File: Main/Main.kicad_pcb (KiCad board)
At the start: 2 copper layers, 76.2 x 76.2 mm, 71 parts, among them J3 Conn_01x03, J4 Conn_01x03, J5 Conn_01x03, J6 Conn_01x03, U1 RP2350A-QFN60, U10 LM75B, U11 MCS1802GS-50-Z, U12 MCS1802GS-50-Z, U13 MCS1802GS-50-Z, U2 W25Q128JVS, U3 AMS1117-3.3, U4 MMC5983MA, U5 ICM-42688-P, U6 INA226, U7 KX134-1211, U8 MS5611-01BA, U9 MCS1802GS-50-Z, Y1 ABM8-272-T3

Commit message: Layout/Footprint Updates
updated footprint of inductor for R-Pi, started planning layout for R-PI components in middle of board, added two options for board size
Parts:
- added G***: LOGO, logos:ECLIPSELogo1, F.Cu at (100.0, 125.0)
- C10, C11, C12, C13, C14, C15, C16, C17, C18, C19, C20, C21, C22, C23, C24, C25, C26, C27, C28, C29, C30, C31, C32, C33, C34, C5, C6, C7, C8, C9: footprint Capacitor_SMD:C_0805_2012Metric -> Capacitor_SMD:C_0603_1608Metric
- L1: footprint Inductor_SMD:L_0805_2012Metric -> otherComponents:AOTA-B201610S3R3-101-T(L_0806_2016metric)
- R10, R11, R12, R2, R3, R4, R5, R6, R7, R8: footprint Resistor_SMD:R_0805_2012Metric -> Resistor_SMD:R_0603_1608Metric
- moved C17 175.9 mm to (108.2, 106.2), turned to 135 degrees
- moved C16 168.9 mm to (104.0, 110.5), turned to -45 degrees
- moved R1 148.8 mm to (98.4, 91.9), turned to -45 degrees
- moved C4 143.7 mm to (104.5, 103.8), turned to -45 degrees
- moved L1 143.0 mm to (96.4, 93.7), turned to 45 degrees
- moved C1 137.1 mm to (98.2, 95.3), turned to 45 degrees
- moved C2 135.0 mm to (97.5, 94.7), turned to 45 degrees
- moved C3 134.9 mm to (99.8, 93.2), turned to -45 degrees
- moved R6 44.3 mm to (103.8, 104.8)
- moved Y1 40.2 mm to (106.2, 108.5), turned to 45 degrees
- moved U4 38.9 mm to (65.3, 57.0)
- moved U5 38.9 mm to (70.6, 62.2)
- moved U7 38.9 mm to (65.8, 64.5)
- moved U8 38.9 mm to (70.3, 55.8)
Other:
- board size 76.2 x 76.2 mm -> 176.9 x 76.2 mm

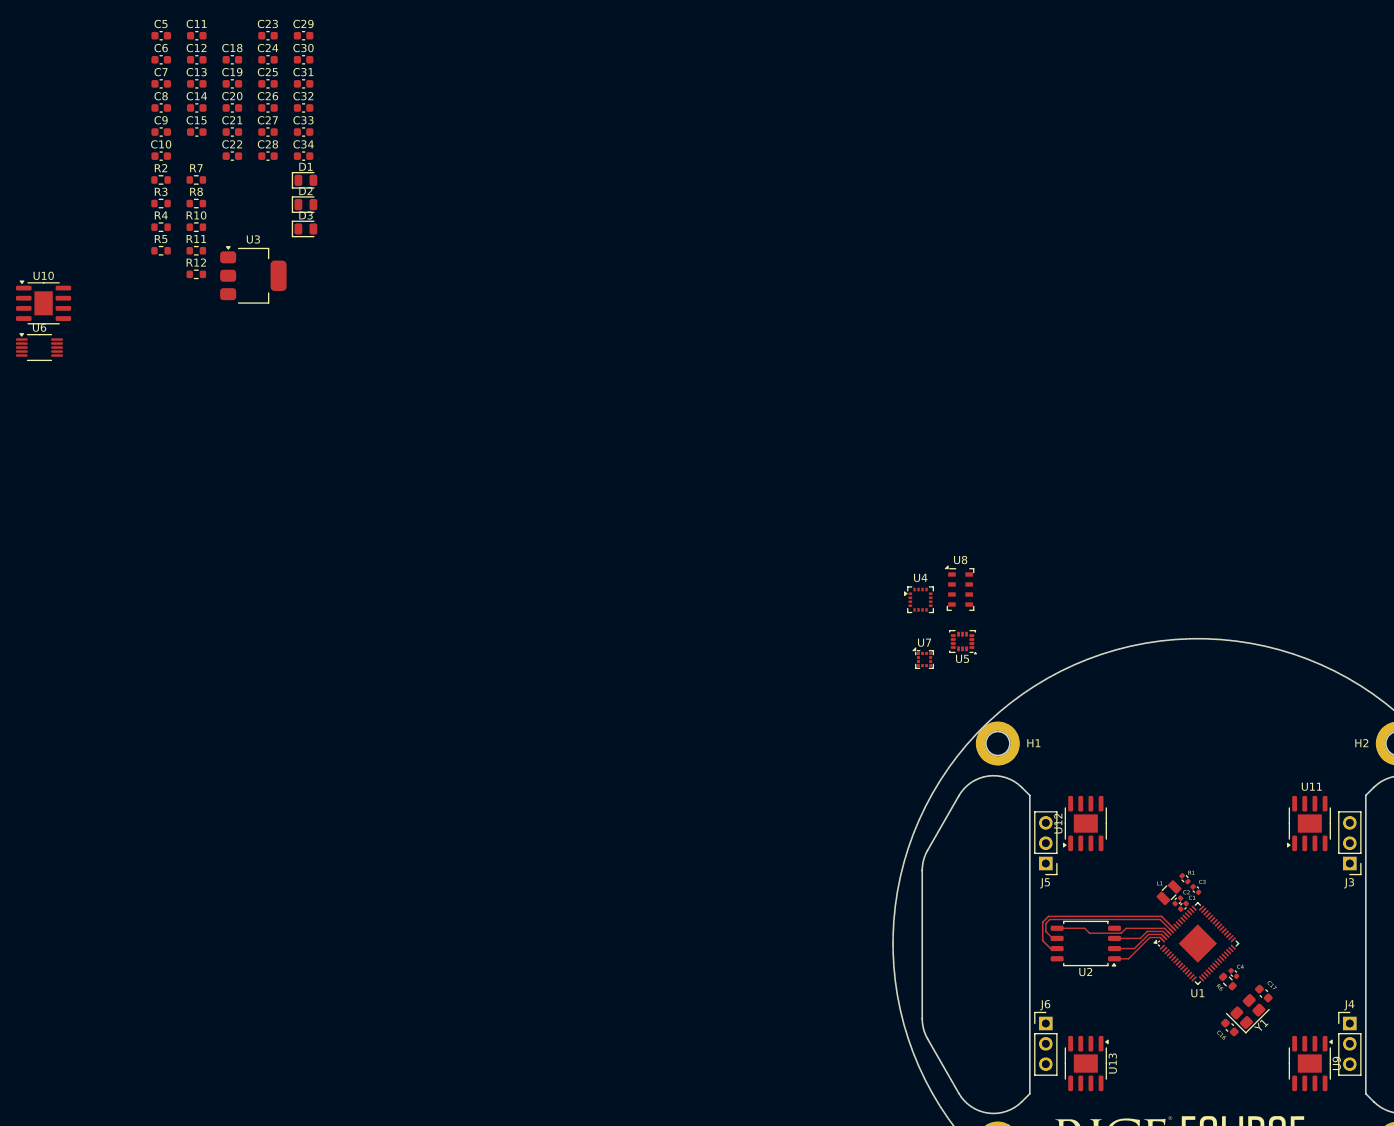
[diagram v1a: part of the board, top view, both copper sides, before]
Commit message: More RP2350 Footprint
put more footprints in place(mostly power), updated things to 0402 where possible, and added switching regulator to schematic
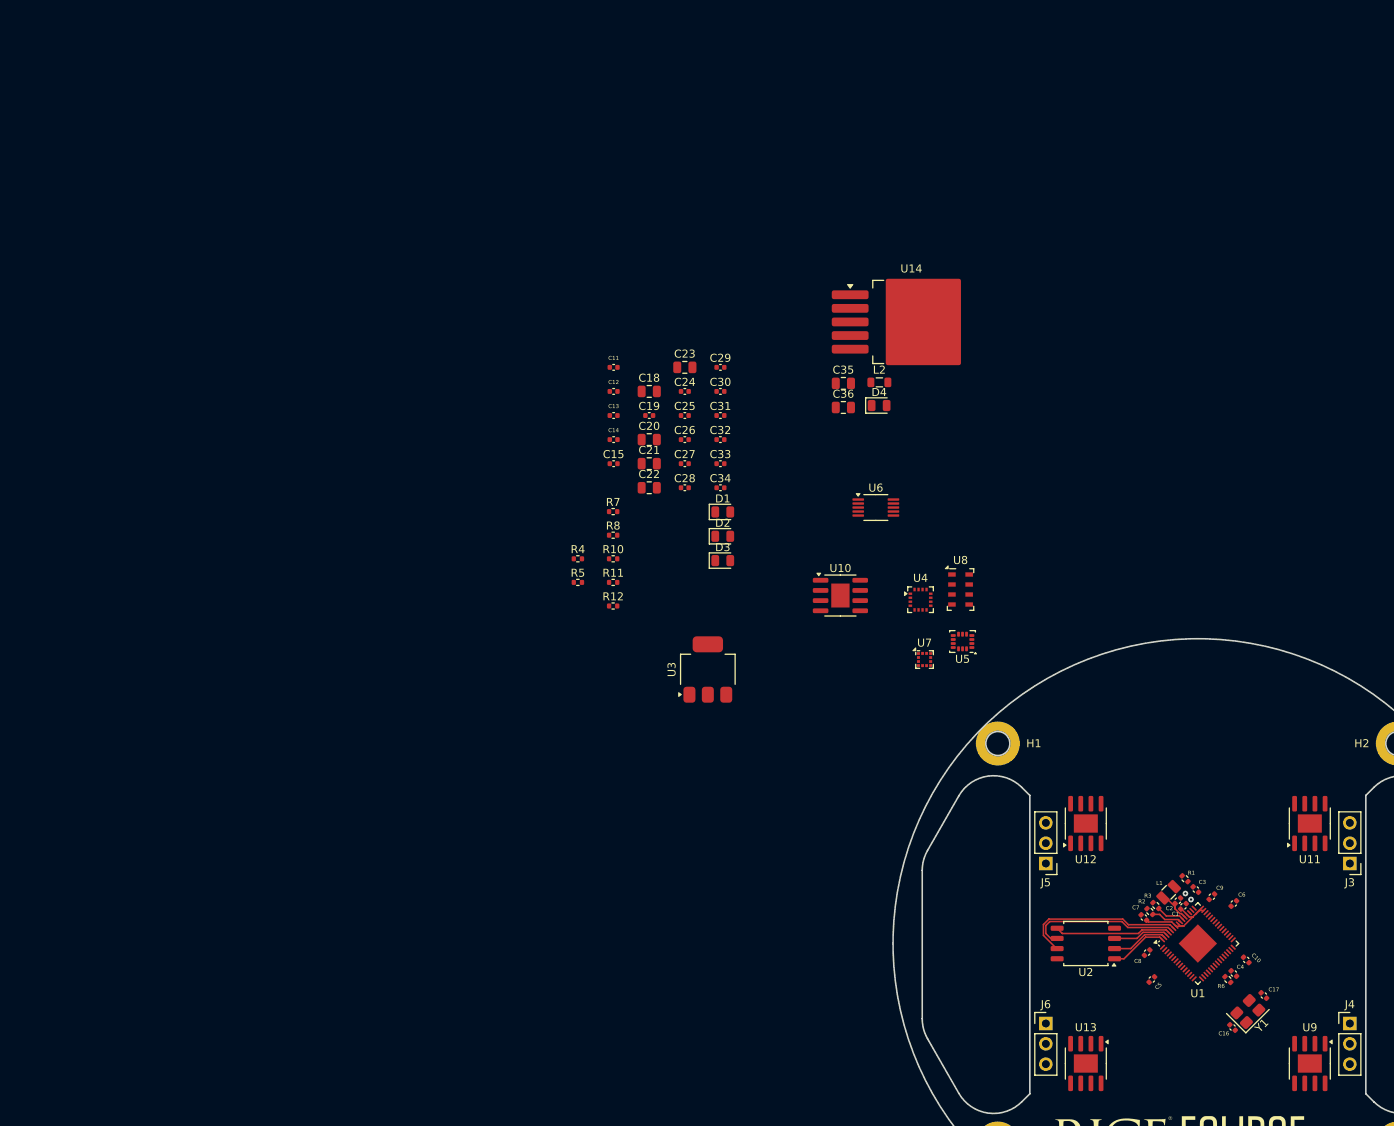
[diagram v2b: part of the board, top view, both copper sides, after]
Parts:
- added C35: 100uF, Capacitor_SMD:C_0805_2012Metric, F.Cu at (55.7, 30.0)
- added C36: 330uF, Capacitor_SMD:C_0805_2012Metric, F.Cu at (55.7, 33.0)
- added D4: 1N5189, Diode_SMD:D_0805_2012Metric, F.Cu at (60.2, 32.8)
- added L2: 330uH, Inductor_SMD:L_0805_2012Metric, F.Cu at (60.2, 29.9)
- added U14: LM2575-3.3BT, Package_TO_SOT_SMD:TO-263-5_TabPin3, F.Cu at (64.2, 22.3)
- C10, C11, C12, C13, C14, C15, C16, C17, C19, C24, C25, C26, C27, C28, C29, C30, C31, C32, C33, C34, C5, C6, C7, C8, C9: footprint Capacitor_SMD:C_0603_1608Metric -> Capacitor_SMD:C_0402_1005Metric
- C18, C20, C21, C22, C23: footprint Capacitor_SMD:C_0603_1608Metric -> Capacitor_SMD:C_0805_2012Metric
- R10, R11, R12, R4, R5, R6, R7, R8: footprint Resistor_SMD:R_0603_1608Metric -> Resistor_SMD:R_0402_1005Metric
- R2, R3: value 27 -> 22; footprint Resistor_SMD:R_0603_1608Metric -> Resistor_SMD:R_0402_1005Metric
- moved C5 171.0 mm to (94.2, 104.5), turned to -135 degrees
- moved C6 170.6 mm to (104.5, 95.0), turned to 45 degrees
- moved C10 168.8 mm to (106.0, 102.0), turned to -45 degrees
- moved C9 162.4 mm to (101.8, 94.2), turned to 45 degrees
- moved C8 162.3 mm to (93.7, 101.1), turned to -135 degrees
- moved C7 161.1 mm to (93.2, 96.8), turned to 135 degrees
- moved R2 153.8 mm to (94.0, 96.0), turned to 135 degrees
- moved R3 152.2 mm to (94.8, 95.2), turned to 135 degrees
- moved U6 106.4 mm to (59.8, 45.5)
- moved U10 106.1 mm to (55.3, 56.5)
- moved U3 75.2 mm to (38.8, 65.8), turned to 90 degrees
- moved C11 66.6 mm to (27.0, 28.0)
- moved C12 66.6 mm to (27.0, 31.0)
- moved C13 66.6 mm to (27.0, 34.0)
- moved C14 66.6 mm to (27.0, 37.0)
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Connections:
- net Net-(U1-USB_DM) renamed /USB-
- net Net-(U1-USB_DP) renamed /USB+
- C28 pad 1: +3V3 -> +3.3V
- R10 pad 2: +3V3 -> +3.3V
- R7 pad 1: +3V3 -> +3.3V
- R8 pad 1: +3V3 -> +3.3V
- U10 pad 8: +3V3 -> +3.3V
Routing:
- net +3.3V: track 0.00 -> 12.1 mm
- net +1V1: track 0.00 -> 4.52 mm
- net /USB+: track 0.00 -> 3.86 mm
- net /USB-: track 0.00 -> 3.61 mm
- net /QSPI_SD3: track 21.8 -> 20.8 mm
- net GND: track 0.00 -> 0.18 mm, vias 0 -> 2
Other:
- copper layers 2 -> 4

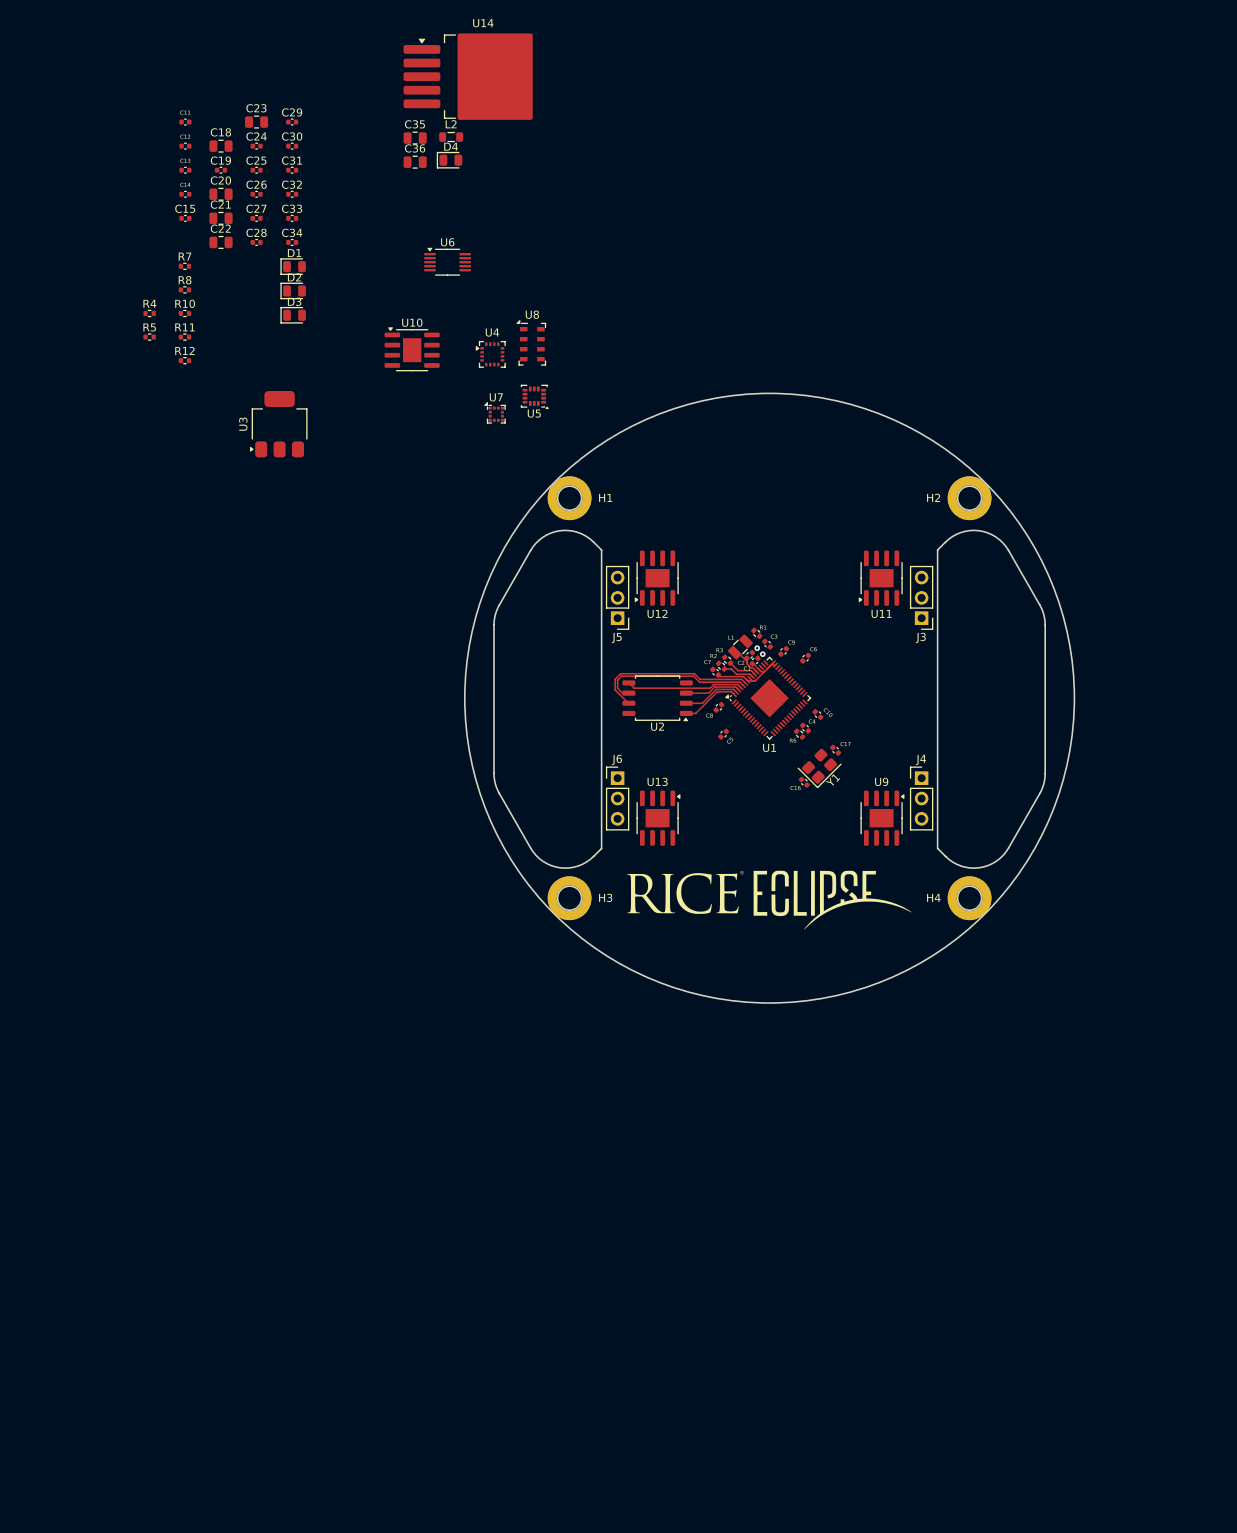
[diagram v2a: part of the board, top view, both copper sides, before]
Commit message: Added 3rd board outline option
new outline without servo cutouts but with one servo wiring hole
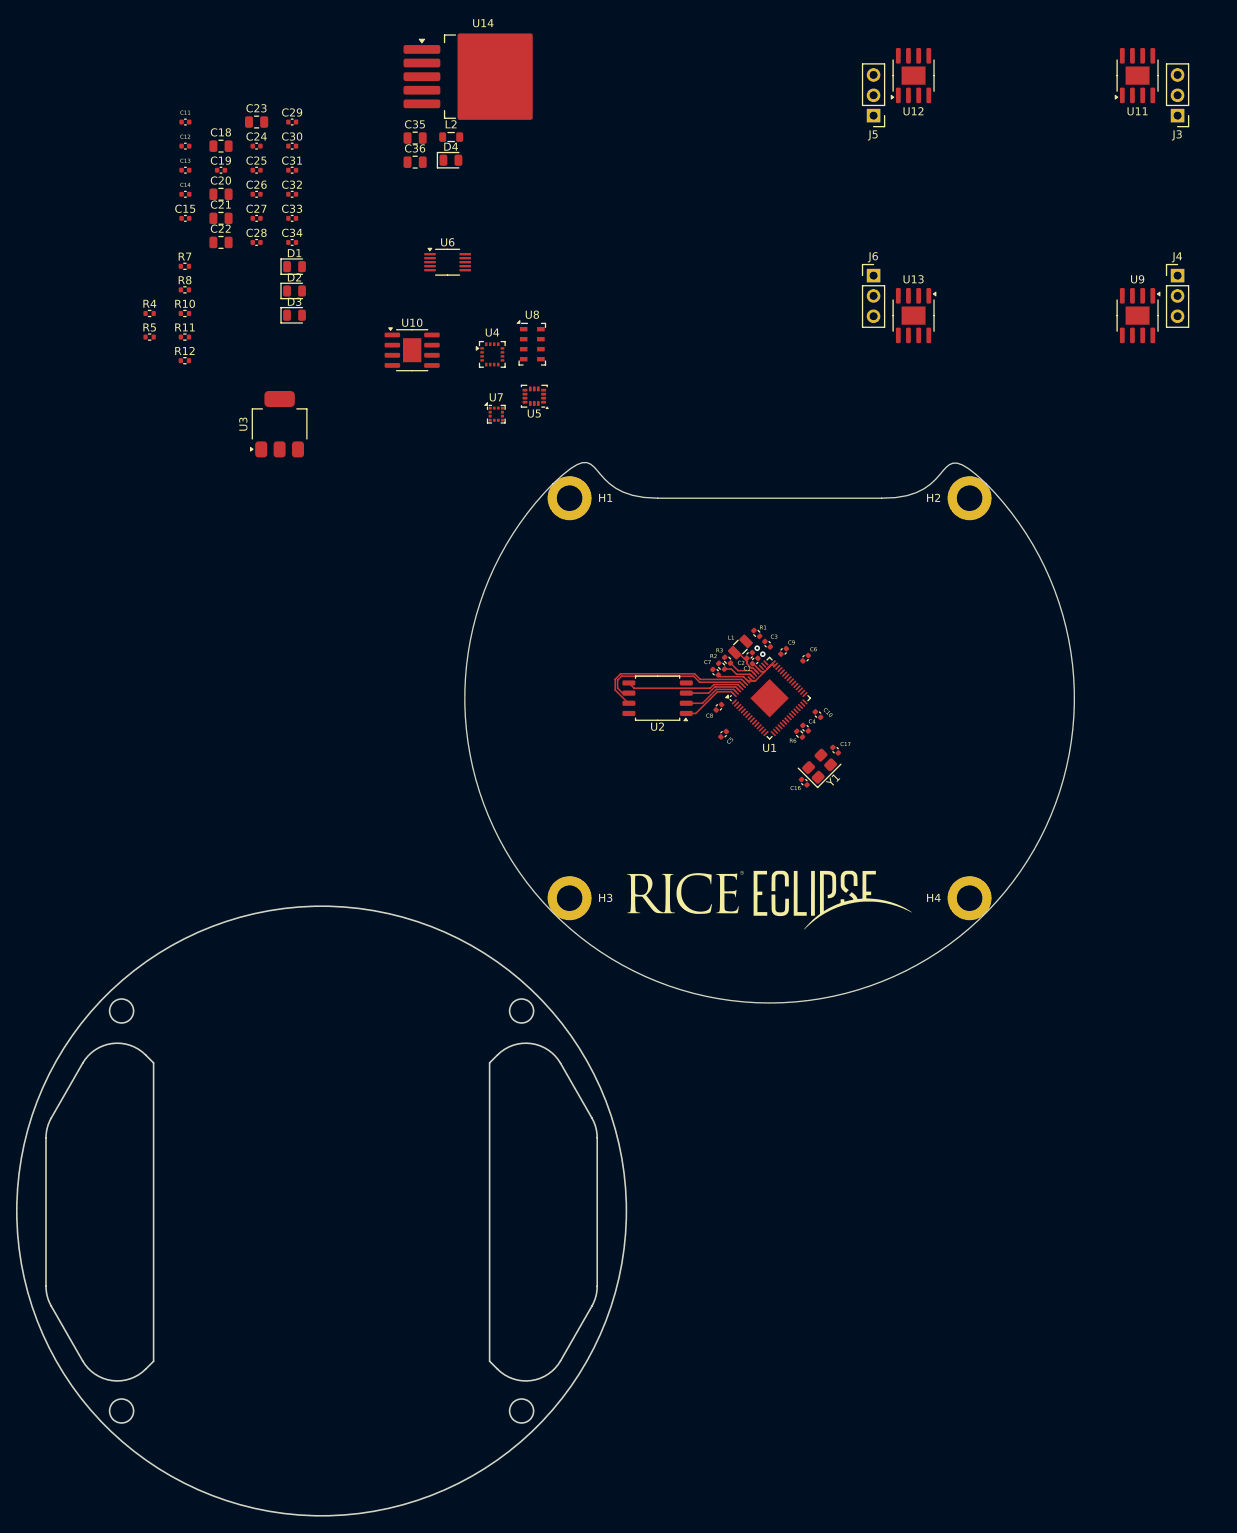
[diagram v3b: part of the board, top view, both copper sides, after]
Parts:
- moved J3 70.5 mm to (151.0, 27.2)
- moved J4 70.5 mm to (151.0, 47.2)
- moved J5 70.5 mm to (113.0, 27.2)
- moved J6 70.5 mm to (113.0, 47.2)
- moved U11 70.5 mm to (146.0, 22.2)
- moved U12 70.5 mm to (118.0, 22.2)
- moved U13 70.5 mm to (118.0, 52.2)
- moved U9 70.5 mm to (146.0, 52.2)
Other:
- board size 176.9 x 76.2 mm -> 232.9 x 138 mm

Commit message: Added shunt footprint and small changes
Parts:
- removed C35: 100uF, Capacitor_SMD:C_0805_2012Metric
- removed C36: 330uF, Capacitor_SMD:C_0805_2012Metric
- removed D4: 1N5189, Diode_SMD:D_0805_2012Metric
- removed L2: 330uH, Inductor_SMD:L_0805_2012Metric
- added R13: 2m, Resistor_SMD:R_1206_3216Metric, F.Cu at (65.4, 45.6)
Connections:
- U6 pad 10: Net-(U6-Vin+) -> VSS
- U6 pad 8: Net-(U6-Vbus) -> GND
- U6 pad 9: Net-(U6-Vbus) -> GND

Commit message: updated before meeting
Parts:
- moved J5 9.41 mm to (117.9, 19.1), turned to 0 degrees
- moved U12 5.48 mm to (112.9, 24.1), turned to -90 degrees
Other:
- board size 232.9 x 138 mm -> 76.2 x 67.6 mm

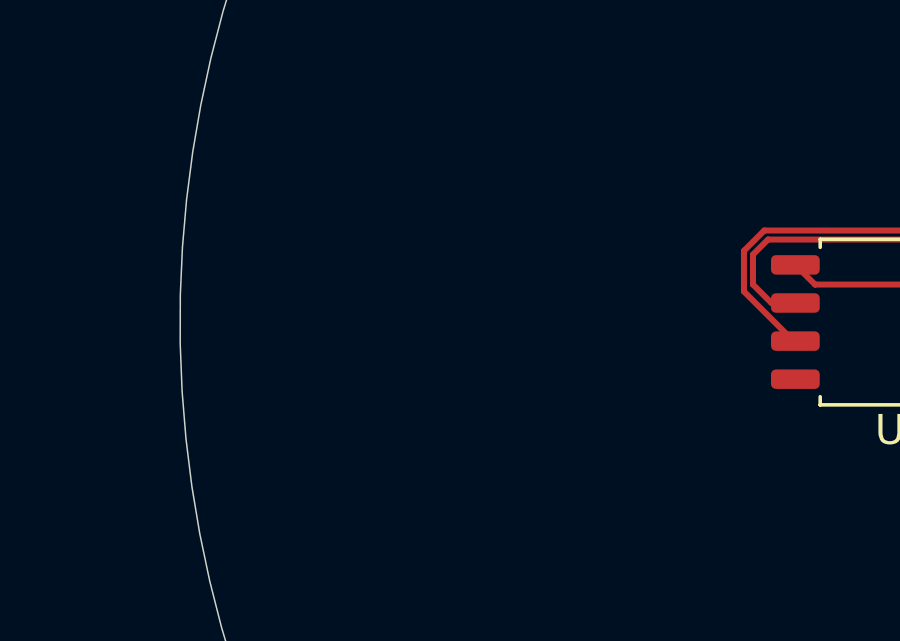
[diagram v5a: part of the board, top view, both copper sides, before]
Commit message: added button footprint
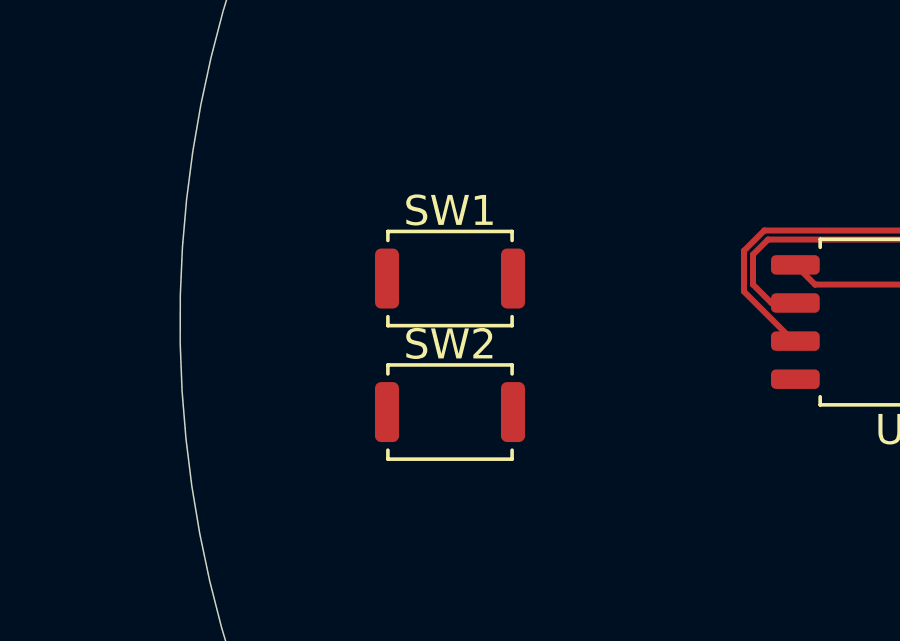
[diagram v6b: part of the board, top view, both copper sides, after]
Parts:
- added SW1: SW_Push, Button_Switch_SMD:SW_Push_SPST_NO_Alps_SKRK, F.Cu at (70.9, 98.5)
- added SW2: SW_Push, Button_Switch_SMD:SW_Push_SPST_NO_Alps_SKRK, F.Cu at (70.9, 103.0)
